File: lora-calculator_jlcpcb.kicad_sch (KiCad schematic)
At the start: 86 parts, among them J1 USB-C, J2 PinHeader_1x04_P2.54mm_Vertic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, J3 LipoCable, SW1 SW_Push, SW10 SW_Push, SW11 SW_Push, SW12 SW_Push, SW13 SW_Push, SW14 SW_Push, SW15 SW_Push, SW16 SW_Push, SW17 SW_Push, SW18 SW_Push, SW19 SW_Push, SW2 SW_Push, SW20 SW_Push, SW21 SW_Push, SW22 SW_Push, SW23 SW_Push, SW24 SW_Push, SW25 SW_Push, SW26 SW_Push, SW27 SW_Push, SW28 SW_Push, SW29 SW_Push, SW3 SW_Push, SW30 SW_Push, SW31 SW_SPDT, SW32 SW_Push, SW33 SW_Push, SW4 SW_Push, SW5 SW_Push, SW6 SW_Push, SW7 SW_Push, SW8 SW_Push, SW9 SW_Push, U1 MCP23017x-x-SO, U3 MCP73831-2-OT, U4 ESP32-C3-WROOM-02U, U5 AP2112K-3.3

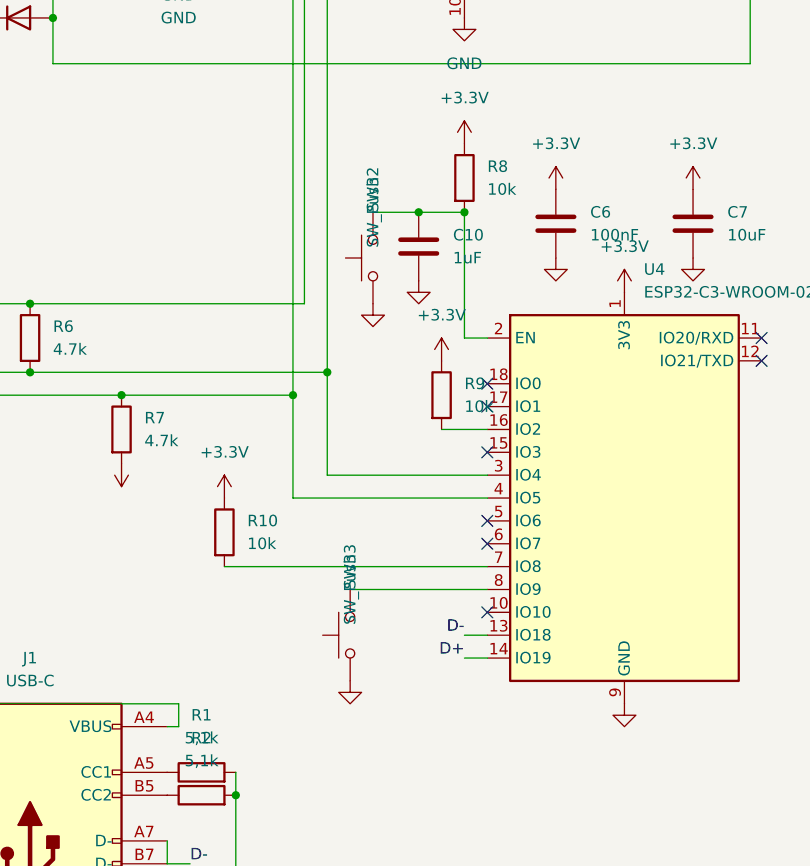
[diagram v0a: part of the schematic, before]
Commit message: Remove SW32 and SW33 reset/boot buttons
Co-Authored-By: Claude Haiku 5.5 <noreply@anthropic.com>
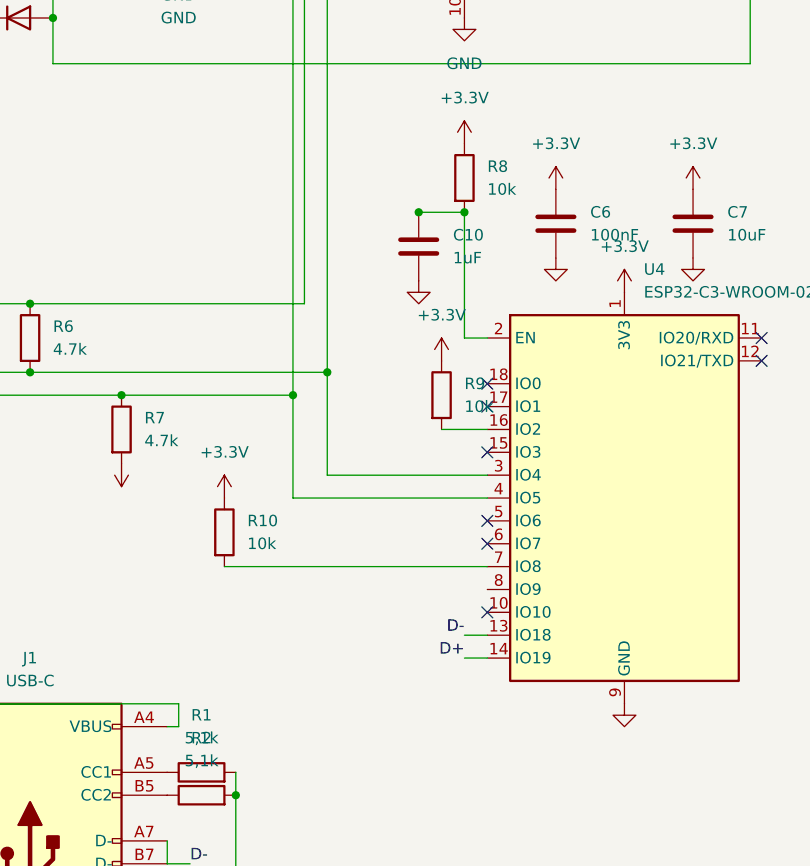
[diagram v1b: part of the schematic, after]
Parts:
- removed SW32, SW33: SW_Push, Button_Switch_SMD:SW_Push_1TS009xxxx-xxxx-xxxx_6x6x5mm, symbol Switch:SW_Push
